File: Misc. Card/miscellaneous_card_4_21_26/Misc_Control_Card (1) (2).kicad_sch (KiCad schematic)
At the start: 44 parts, among them IC2Port1 Conn_01x02, IC2Port2 Conn_01x02, IC2Port3 Conn_01x02, J1 Conn_01x03_Pin, J2 Conn_01x02, J3 Conn_01x02, J4 Conn_01x02, J5 Conn_01x02, J7 Screw_Terminal_01x02, J8 Conn_01x03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

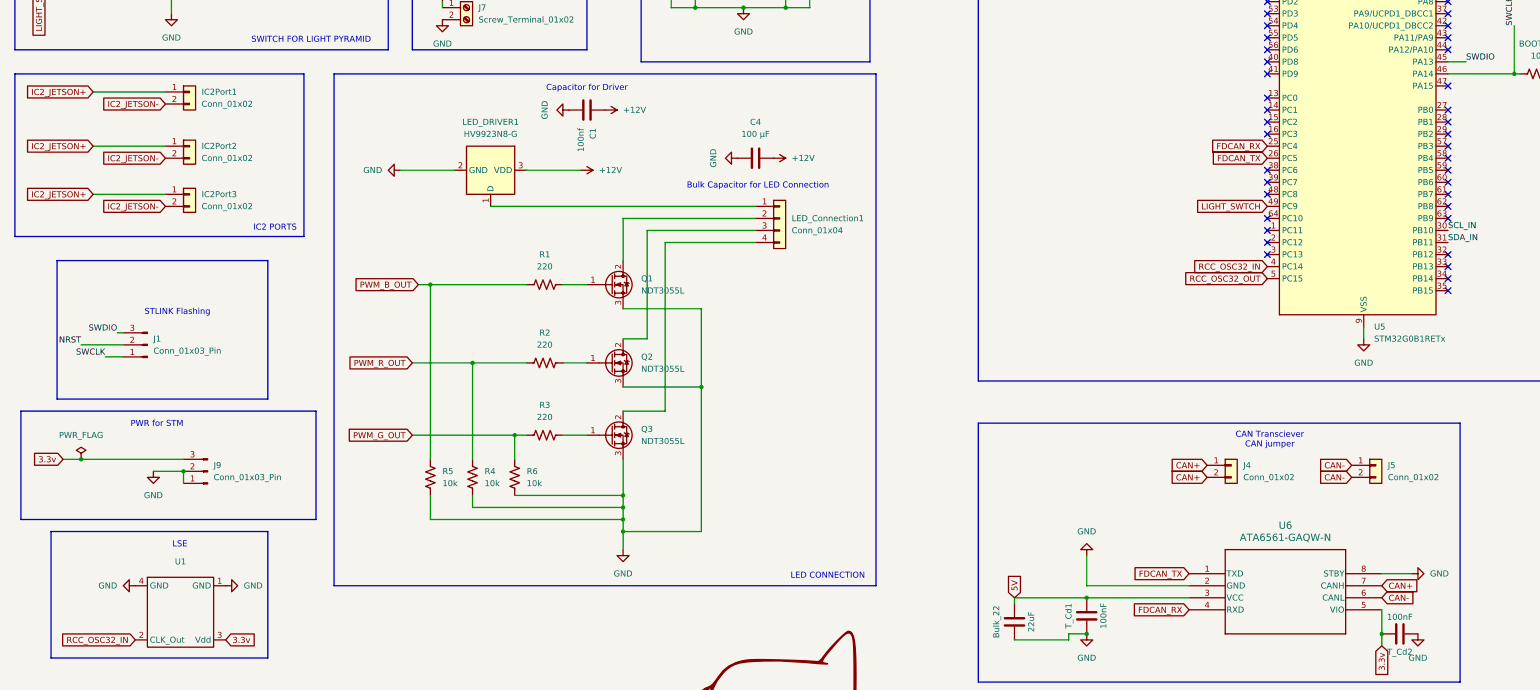
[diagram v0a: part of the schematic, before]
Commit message: Added CAN Impedance Matching
Misc Card
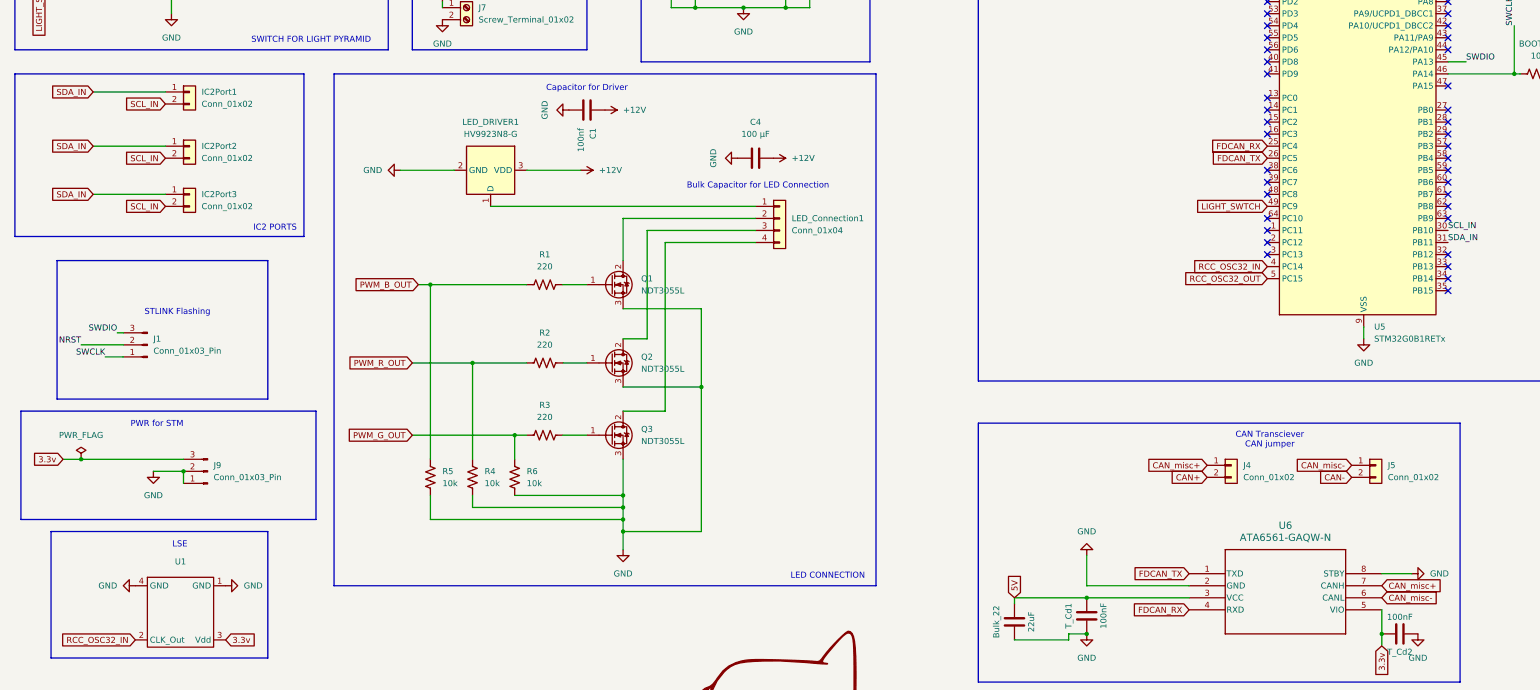
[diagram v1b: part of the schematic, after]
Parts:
- J3: footprint Connector_PinHeader_2.54mm:PinHeader_1x02_P2.54mm_Vertical -> Connector_JST:JST_PH_B2B-PH-K_1x02_P2.00mm_Vertical
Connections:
- net IC2_JETSON+ is gone; now on net SDA_IN: IC2Port1.1 (Pin_1), IC2Port2.1 (Pin_1), IC2Port3.1 (Pin_1)
- net IC2_JETSON- is gone; now on net SCL_IN: IC2Port1.2 (Pin_2), IC2Port2.2 (Pin_2), IC2Port3.2 (Pin_2)
- net CAN+: no longer J4.1 (Pin_1), U6.7 (CANH)
- net CAN-: no longer J5.1 (Pin_1), U6.6 (CANL)
- new net CAN_misc+: J4.1 (Pin_1), U6.7 (CANH)
- new net CAN_misc-: J5.1 (Pin_1), U6.6 (CANL)
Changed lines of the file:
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@@
 		)
 	)
+	(global_label "SDA_IN"
+		(shape input)
+		(at 102.87 219.71 180)
+		(fields_autoplaced yes)
+		(effects
+			(font
+				(size 1.27 1.27)
+			)
+			(justify right)
+		)
+		(property "Intersheetrefs" "${INTERSHEET_REFS}"
+			(at 93.4138 219.71 0)
+			(effects
+				(font
+					(size 1.27 1.27)
+				)
+				(justify right)
+				(hide yes)
+			)
+		)
+	)
 	(global_label "USART1-"
 		(shape input)
@@
 		)
 	)
-	(global_label "RCC_OSC32_IN"
+	(global_label "SDA_IN"
 		(shape input)
-		(at 350.52 256.54 180)
+		(at 102.87 231.14 180)
 		(fields_autoplaced yes)
 		(effects
@@
 		)
 		(property "Intersheetrefs" "${INTERSHEET_REFS}"
-			(at 333.6253 256.54 0)
+			(at 93.4138 231.14 0)
 			(effects
 				(font
@@
 		)
 	)
-	(global_label "IC2_JETSON-"
+	(global_label "RCC_OSC32_IN"
 		(shape input)
-		(at 118.11 222.25 180)
+		(at 350.52 256.54 180)
 		(fields_autoplaced yes)
 		(effects
@@
 		)
 		(property "Intersheetrefs" "${INTERSHEET_REFS}"
-			(at 102.5458 222.25 0)
+			(at 333.6253 256.54 0)
 			(effects
 				(font
@@
 		)
 	)
-	(global_label "CAN+"
+	(global_label "CAN_misc+"
 		(shape input)
 		(at 374.65 323.85 0)
@@
 		)
 		(property "Intersheetrefs" "${INTERSHEET_REFS}"
-			(at 382.8967 323.85 0)
+			(at 388.2791 323.85 0)
 			(effects
 				(font
@@
 		)
 	)
-	(global_label "IC2_JETSON+"
+	(global_label "3.3v"
 		(shape input)
-		(at 102.87 241.3 180)
+		(at 374.65 336.55 270)
 		(fields_autoplaced yes)
 		(effects
@@
 		)
 		(property "Intersheetrefs" "${INTERSHEET_REFS}"
-			(at 87.3058 241.3 0)
+			(at 374.65 343.5266 90)
 			(effects
 				(font
@@
 		)
 	)
-	(global_label "3.3v"
+	(global_label "SCL_IN"
 		(shape input)
-		(at 374.65 336.55 270)
+		(at 118.11 222.25 180)
 		(fields_autoplaced yes)
 		(effects
@@
 		)
 		(property "Intersheetrefs" "${INTERSHEET_REFS}"
-			(at 374.65 343.5266 90)
+			(at 108.7143 222.25 0)
 			(effects
 				(font
@@
 		)
 	)
-	(global_label "IC2_JETSON-"
-		(shape input)
-		(at 118.11 233.68 180)
-		(fields_autoplaced yes)
-		(effects
-			(font
-				(size 1.27 1.27)
-			)
-			(justify right)
-		)
-		(property "Intersheetrefs" "${INTERSHEET_REFS}"
-			(at 102.5458 233.68 0)
-			(effects
-				(font
-					(size 1.27 1.27)
-				)
-				(justify right)
-				(hide yes)
-			)
-		)
-	)
 	(global_label "USART1+"
 		(shape input)
@@
 		)
 	)
-	(global_label "IC2_JETSON+"
+	(global_label "RCC_OSC32_IN"
 		(shape input)
-		(at 102.87 219.71 180)
+		(at 111.76 335.28 180)
 		(fields_autoplaced yes)
 		(effects
@@
 		)
 		(property "Intersheetrefs" "${INTERSHEET_REFS}"
-			(at 87.3058 219.71 0)
+			(at 94.8653 335.28 0)
 			(effects
 				(font
@@
 		)
 	)
-	(global_label "RCC_OSC32_IN"
+	(global_label "SCL_IN"
 		(shape input)
-		(at 111.76 335.28 180)
+		(at 118.11 233.68 180)
 		(fields_autoplaced yes)
 		(effects
@@
 		)
 		(property "Intersheetrefs" "${INTERSHEET_REFS}"
-			(at 94.8653 335.28 0)
+			(at 108.7143 233.68 0)
 			(effects
 				(font
@@
 		)
 	)
-	(global_label "CAN-"
+	(global_label "CAN_misc-"
 		(shape input)
 		(at 368.3 298.45 180)
@@
 		)
 		(property "Intersheetrefs" "${INTERSHEET_REFS}"
-			(at 360.0533 298.45 0)
-			(effects
-				(font
-					(size 1.27 1.27)
-				)
-				(justify right)
-				(hide yes)
-			)
-		)
-	)
-	(global_label "IC2_JETSON+"
-		(shape input)
-		(at 102.87 231.14 180)
-		(fields_autoplaced yes)
-		(effects
-			(font
-				(size 1.27 1.27)
-			)
-			(justify right)
-		)
-		(property "Intersheetrefs" "${INTERSHEET_REFS}"
-			(at 87.3058 231.14 0)
+			(at 354.6709 298.45 0)
 			(effects
 				(font
@@
 		)
 	)
-	(global_label "CAN+"
+	(global_label "CAN_misc+"
 		(shape input)
 		(at 337.82 298.45 180)
@@
 		)
 		(property "Intersheetrefs" "${INTERSHEET_REFS}"
-			(at 329.5733 298.45 0)
+			(at 324.1909 298.45 0)
 			(effects
 				(font
@@
 		)
 	)
-	(global_label "CAN-"
+	(global_label "CAN_misc-"
 		(shape input)
 		(at 374.65 326.39 0)
@@
 		)
 		(property "Intersheetrefs" "${INTERSHEET_REFS}"
-			(at 382.8967 326.39 0)
+			(at 388.2791 326.39 0)
 			(effects
 				(font
@@
 		)
 	)
-	(global_label "IC2_JETSON-"
-		(shape input)
-		(at 118.11 243.84 180)
-		(fields_autoplaced yes)
-		(effects
-			(font
-				(size 1.27 1.27)
-			)
-			(justify right)
-		)
-		(property "Intersheetrefs" "${INTERSHEET_REFS}"
-			(at 102.5458 243.84 0)
-			(effects
-				(font
-					(size 1.27 1.27)
-				)
-				(justify right)
-				(hide yes)
-			)
-		)
-	)
 	(global_label "3.3v"
 		(shape input)
@@
 		)
 	)
+	(global_label "SCL_IN"
+		(shape input)
+		(at 118.11 243.84 180)
+		(fields_autoplaced yes)
+		(effects
+			(font
+				(size 1.27 1.27)
+			)
+			(justify right)
+		)
+		(property "Intersheetrefs" "${INTERSHEET_REFS}"
+			(at 108.7143 243.84 0)
+			(effects
+				(font
+					(size 1.27 1.27)
+				)
+				(justify right)
+				(hide yes)
+			)
+		)
+	)
+	(global_label "SDA_IN"
+		(shape input)
+		(at 102.87 241.3 180)
+		(fields_autoplaced yes)
+		(effects
+			(font
+				(size 1.27 1.27)
+			)
+			(justify right)
+		)
+		(property "Intersheetrefs" "${INTERSHEET_REFS}"
+			(at 93.4138 241.3 0)
+			(effects
+				(font
+					(size 1.27 1.27)
+				)
+				(justify right)
+				(hide yes)
+			)
+		)
+	)
 	(symbol
 		(lib_id "custom_components:SiT1552")
@@
 			)
 		)
-		(property "Footprint" "Connector_PinHeader_2.54mm:PinHeader_1x02_P2.54mm_Vertical"
+		(property "Footprint" "Connector_JST:JST_PH_B2B-PH-K_1x02_P2.00mm_Vertical"
 			(at 147.32 152.4 0)
 			(effects
